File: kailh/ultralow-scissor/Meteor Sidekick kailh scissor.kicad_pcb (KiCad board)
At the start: 2 copper layers, 166 x 75 mm, 89 parts, among them K1 KEYSW, K10 KEYSW, K11 KEYSW, K12 KEYSW, K13 KEYSW, K14 KEYSW, K15 KEYSW, K16 KEYSW, K17 KEYSW, K18 KEYSW, K19 KEYSW, K2 KEYSW, K20 KEYSW, K21 KEYSW, K22 KEYSW, K23 KEYSW, K24 KEYSW, K25 KEYSW, K26 KEYSW, K27 KEYSW, K28 KEYSW, K29 KEYSW, K3 KEYSW, K30 KEYSW, K31 KEYSW, K32 KEYSW, K33 KEYSW, K34 KEYSW, K35 KEYSW, K36 KEYSW, K37 KEYSW, K38 KEYSW, K39 KEYSW, K4 KEYSW, K40 KEYSW, K5 KEYSW, K6 KEYSW, K7 KEYSW, K8 KEYSW, K9 KEYSW, U1 nice_nano_v2

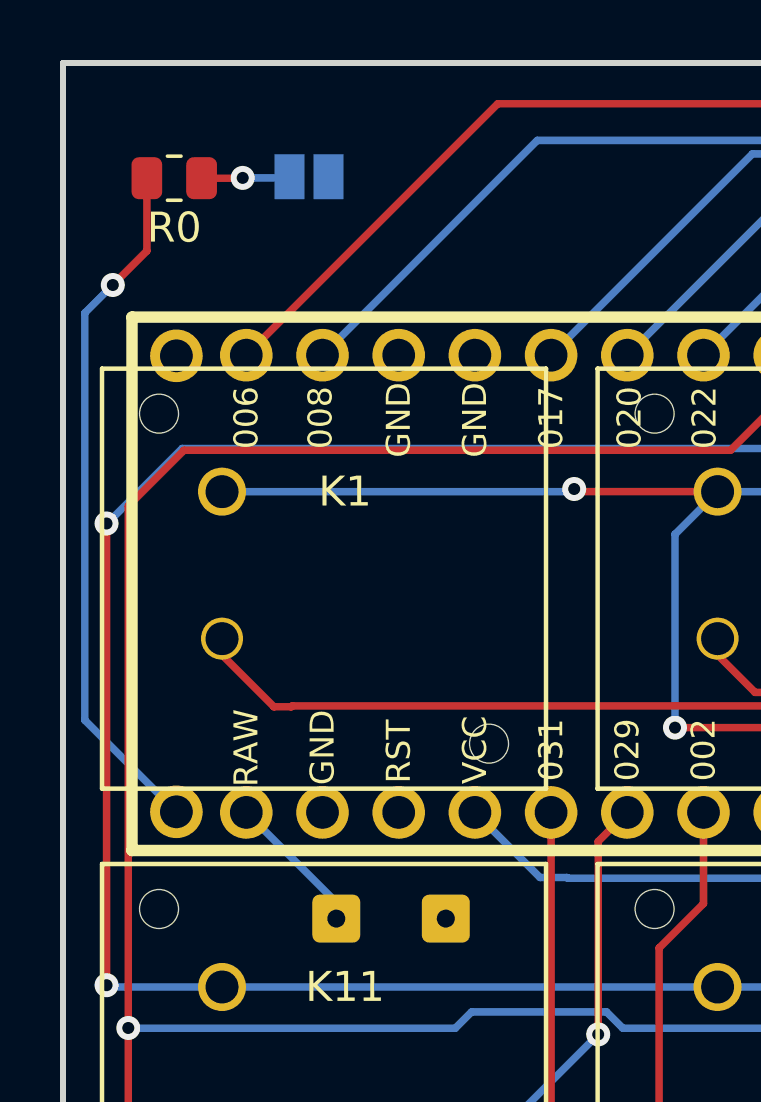
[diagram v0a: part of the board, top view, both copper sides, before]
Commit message: Fixed reset and batt on isolated gnd
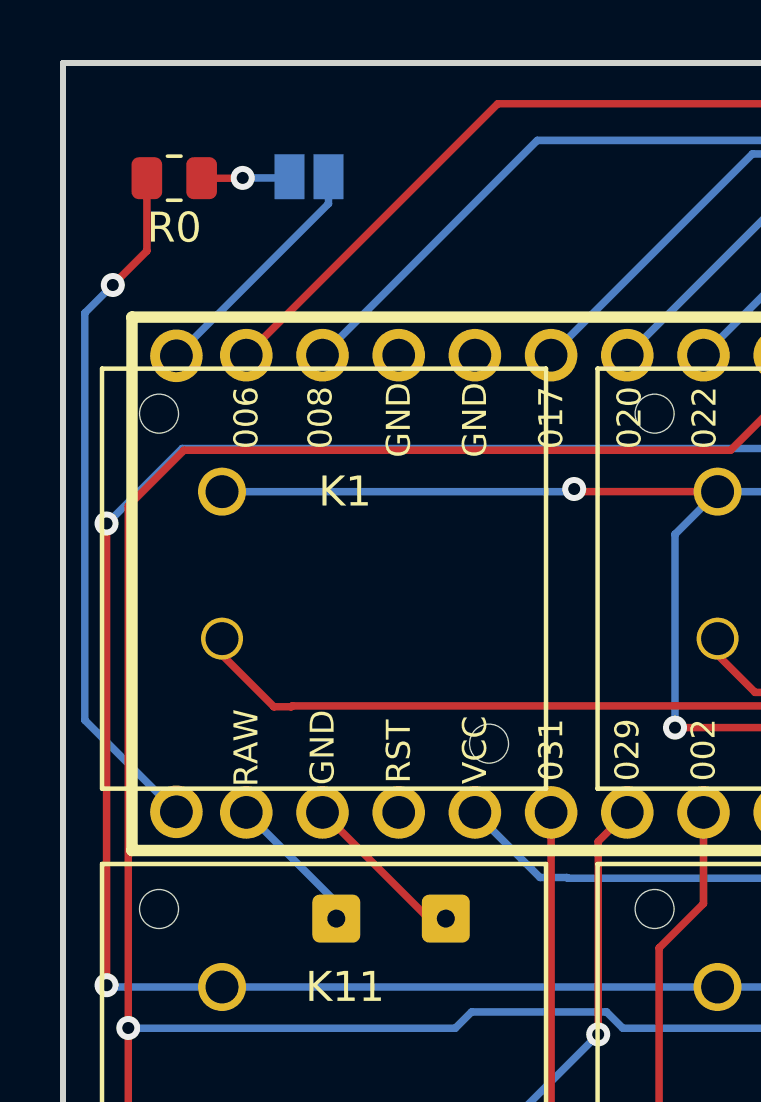
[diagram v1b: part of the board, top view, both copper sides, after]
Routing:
- net /GND: track 0.00 -> 13.6 mm
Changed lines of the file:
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@@
   (segment (start 91.826656 90.158009) (end 93.213647 91.545) (width 0.25) (layer "F.Cu") (net 37))
   (segment (start 93.213647 91.545) (end 95.1712 91.545) (width 0.25) (layer "F.Cu") (net 37))
+  (segment (start 32.64 48.965) (end 29.1 45.425) (width 0.25) (layer "F.Cu") (net 38))
+  (segment (start 33.21 48.965) (end 32.64 48.965) (width 0.25) (layer "F.Cu") (net 38))
+  (segment (start 29.3 25.135) (end 24.23 30.205) (width 0.25) (layer "B.Cu") (net 38))
+  (segment (start 29.3 24.235) (end 29.3 25.135) (width 0.25) (layer "B.Cu") (net 38))
   (segment (start 111.694625 91.55) (end 112.719625 92.575) (width 0.25) (layer "F.Cu") (net 39))
   (segment (start 109.737535 91.55) (end 111.694625 91.55) (width 0.25) (layer "F.Cu") (net 39))

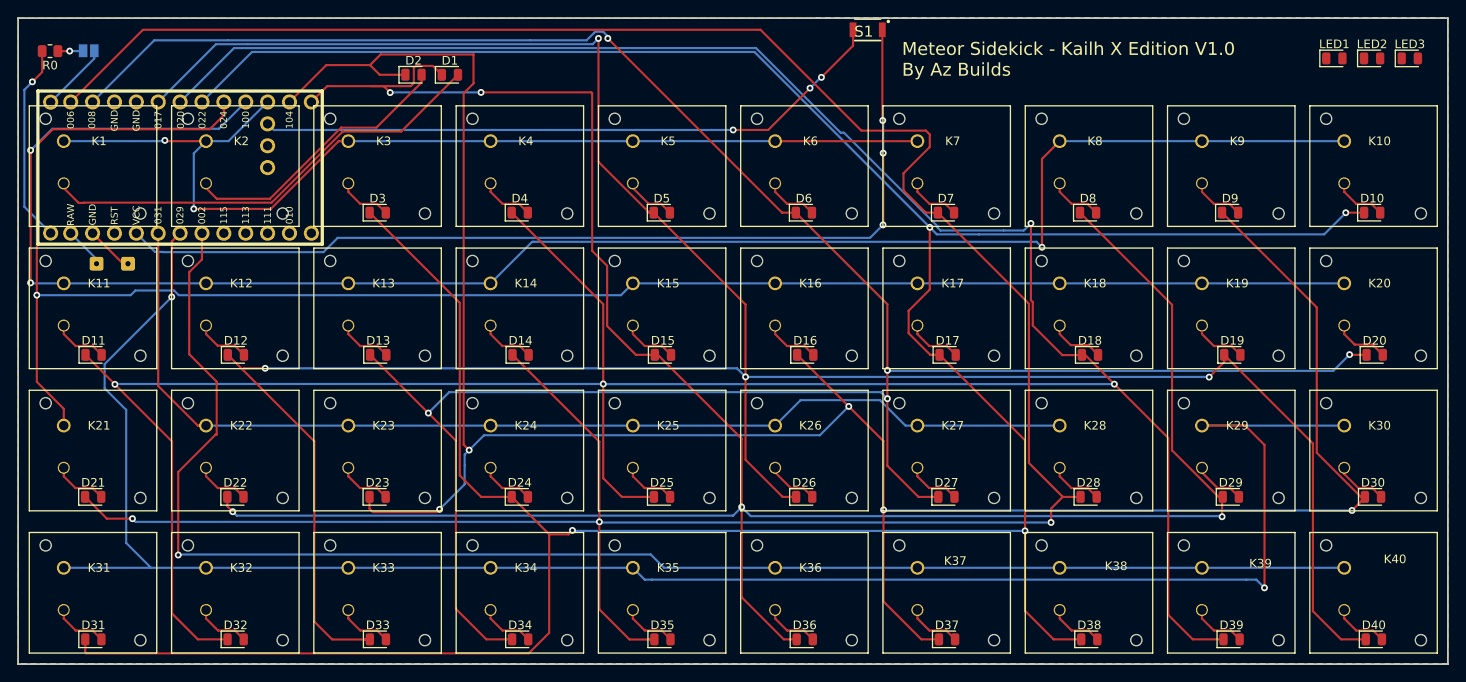
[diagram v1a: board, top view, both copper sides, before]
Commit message: Fixed missed connections
Reset now connected
LEDs now connected
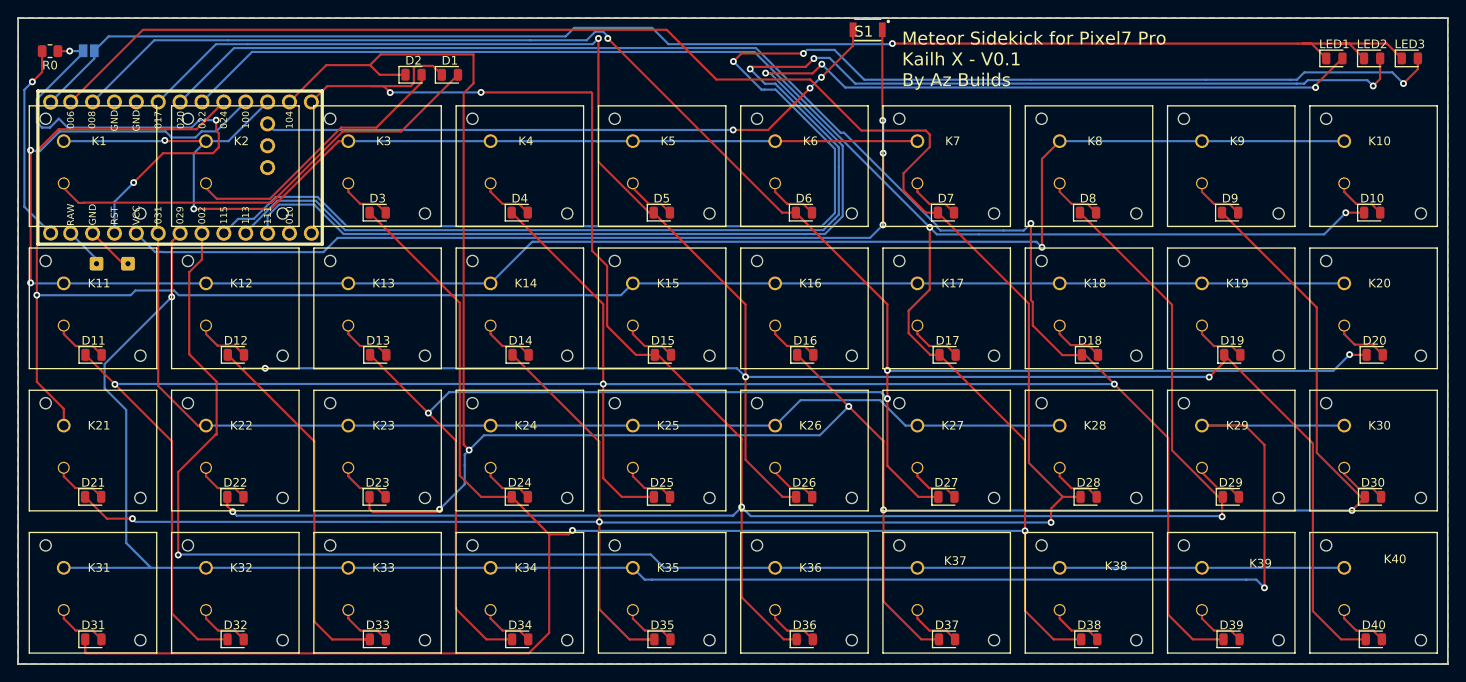
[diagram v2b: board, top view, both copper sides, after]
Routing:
- net /LED3: track 0.00 -> 182.5 mm, vias 0 -> 3
- net /LED2: track 0.00 -> 172.6 mm, vias 0 -> 3
- net /LED1: track 0.00 -> 162.3 mm, vias 0 -> 3
- net /GND: track 13.6 -> 175.0 mm, vias 0 -> 1
- net /RESET: track 2.95 -> 57.5 mm, vias 1 -> 3
- net /row_2: track 211.4 -> 210.1 mm
- net /row_1: track 208.6 -> 209.4 mm
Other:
- board text added: "Meteor Sidekick for Pixel7 Pro Kailh X - V0.1 By Az Builds"
- board text removed: "Meteor Sidekick - Kailh X Edition V1.0 By Az Builds"
